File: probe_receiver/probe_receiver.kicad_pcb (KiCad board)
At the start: 2 copper layers, 32 x 32 mm, 9 parts, among them J1 Conn_01x05_Female, K1 HE721C0510, Q1 2N2907A, U1 TSSP4038

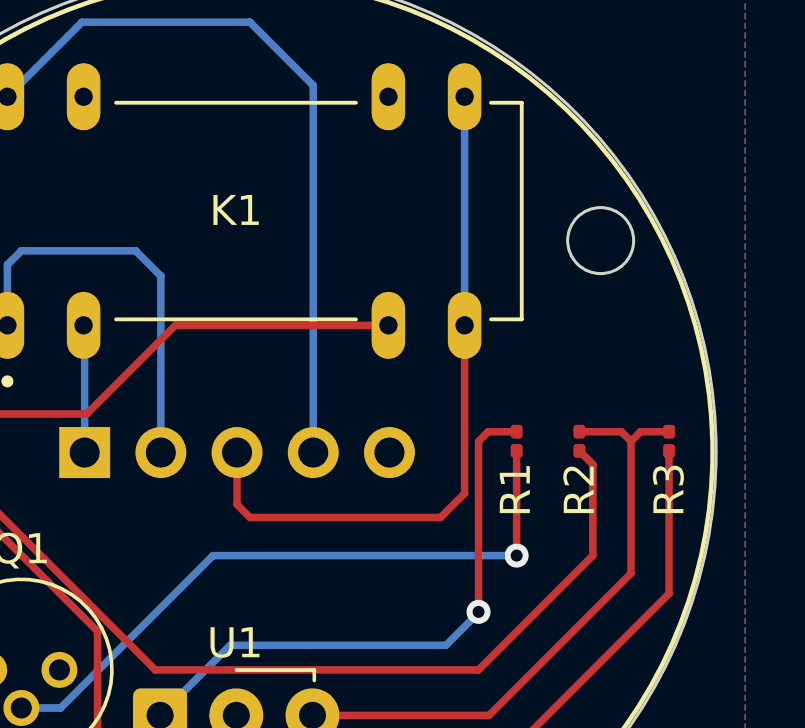
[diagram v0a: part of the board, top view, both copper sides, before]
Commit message: - add fix for PCB v1.1 (fix resistor place 1608)
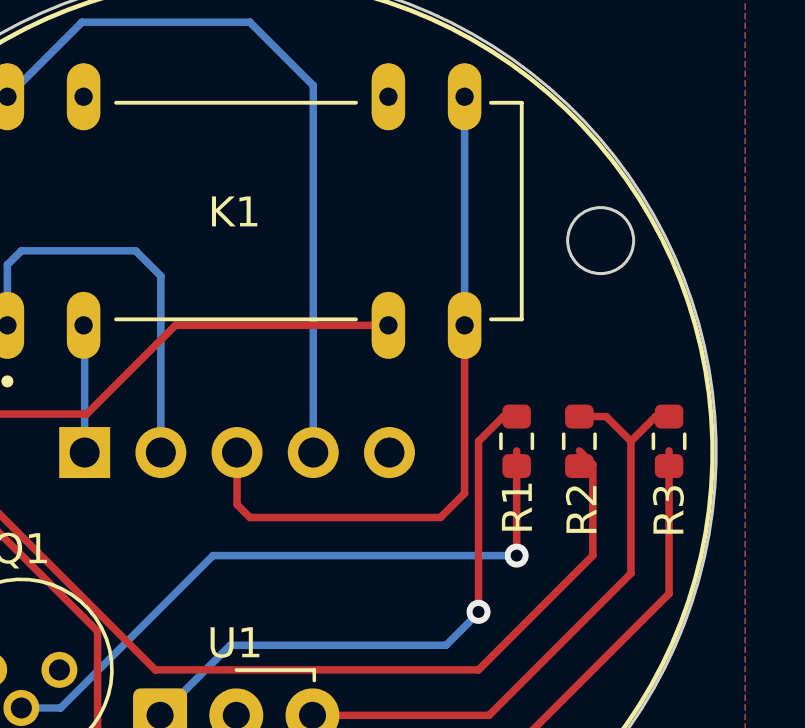
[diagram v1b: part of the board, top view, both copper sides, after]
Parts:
- added  : Probe Reciver v1.1, LOGO, B.Cu at (100.4, 89.2)
- R1, R2, R3: footprint Resistor_SMD:R_0201_0603Metric -> Resistor_SMD:R_0603_1608Metric

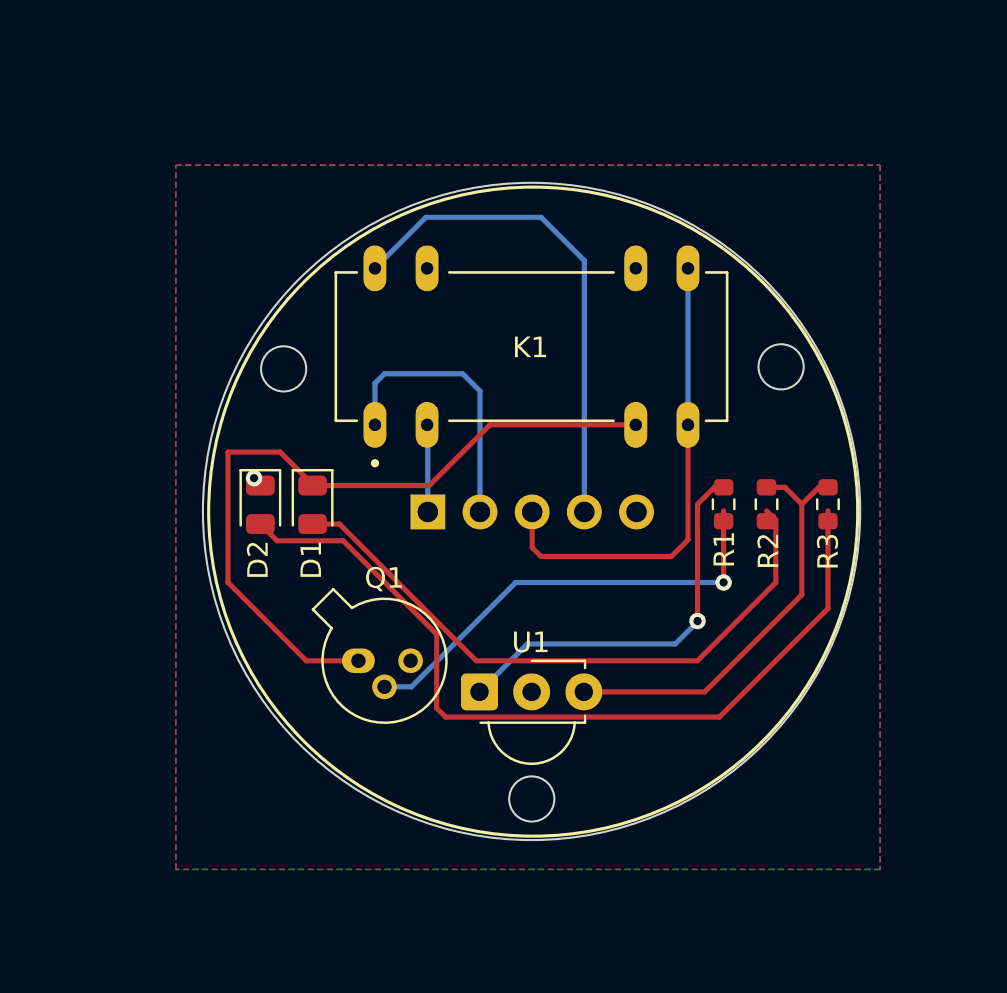
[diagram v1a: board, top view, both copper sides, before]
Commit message: - update probe reciver to v1.1
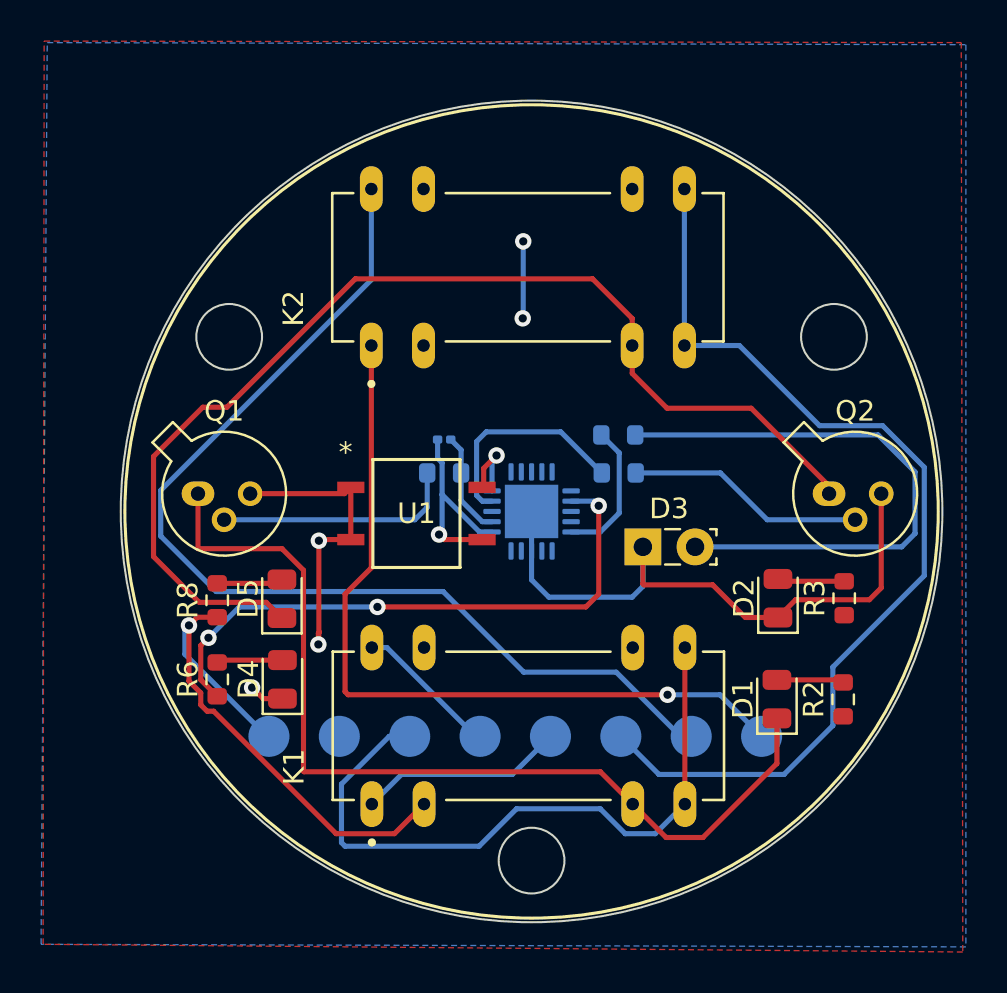
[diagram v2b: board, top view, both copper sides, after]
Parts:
- removed  : Probe Reciver v1.1, LOGO
- removed J1: Conn_01x05_Female, Connector_PinSocket_2.54mm:PinSocket_1x05_P2.54mm_Vertical
- added 5V1: TestPoint, TestPoint:TestPoint_Pad_D2.0mm, B.Cu at (87.2, 111.0)
- added D3: IRL81A, LED_THT:LED_SideEmitter_Rectangular_W4.5mm_H1.6mm, F.Cu at (105.4, 101.7)
- added D4: LED_YELLOW, LED_SMD:LED_0805_2012Metric, F.Cu at (87.9, 108.2)
- added D5: LED_ERR, LED_SMD:LED_0805_2012Metric, F.Cu at (87.8, 104.2)
- added EC1: TestPoint, TestPoint:TestPoint_Pad_D2.0mm, B.Cu at (111.2, 111.0)
- added EO1: TestPoint, TestPoint:TestPoint_Pad_D2.0mm, B.Cu at (107.8, 111.0)
- added ERR1: TestPoint, TestPoint:TestPoint_Pad_D2.0mm, B.Cu at (104.3, 111.0)
- added GND1: TestPoint, TestPoint:TestPoint_Pad_D2.0mm, B.Cu at (90.6, 111.0)
- added IN1: TestPoint, TestPoint:TestPoint_Pad_D2.0mm, B.Cu at (94.1, 111.0)
- added K2: HE721C0510, HE721C0510:RELAY_HE721C0510, F.Cu at (99.8, 88.1)
- added NC1: TestPoint, TestPoint:TestPoint_Pad_D2.0mm, B.Cu at (100.9, 111.0)
- added NO1: TestPoint, TestPoint:TestPoint_Pad_D2.0mm, B.Cu at (97.5, 111.0)
- added Q2: 2N2907A, Package_TO_SOT_THT:TO-18-3, F.Cu at (114.5, 99.1)
- added R4: R1K, Resistor_SMD:R_0603_1608Metric, B.Cu at (104.2, 96.3)
- added R5: R0, Resistor_SMD:R_0201_0603Metric, B.Cu at (95.7, 96.5)
- added R6: R1K, Resistor_SMD:R_0603_1608Metric, F.Cu at (84.7, 108.2)
- added R7: R39, Resistor_SMD:R_0603_1608Metric, B.Cu at (104.2, 98.1)
- added R8: R1K, Resistor_SMD:R_0603_1608Metric, F.Cu at (84.7, 104.3)
- added U2: ATtiny85-20M, Package_DFN_QFN:QFN-20-1EP_4x4mm_P0.5mm_EP2.6x2.6mm, B.Cu at (100.0, 100.0)
- D1: value LED -> LED_SIGN
- D2: value LED -> LED_POW
- R1: moved to B.Cu
- U1: value TSSP4038 -> IRM-H638T/TR2; footprint OptoDevice:Vishay_MINICAST-3Pin -> IRM-H638T-TR2:IRM-H638T&slash_TR2_EVE
- moved D2 25.6 mm to (112.0, 104.2), turned to 90 degrees
- moved D1 24.5 mm to (111.9, 109.1), turned to 90 degrees
- moved K1 18.5 mm to (99.8, 110.4)
- moved R1 13.7 mm to (95.7, 98.1), turned to 180 degrees
- moved Q1 11.3 mm to (83.8, 99.1)
- moved R2 10.2 mm to (115.2, 109.2), turned to 90 degrees
- moved U1 9.21 mm to (94.4, 100.1)
- moved R3 4.64 mm to (115.2, 104.2), turned to 90 degrees
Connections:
- U1 pad 1: Net-(R1-Pad1) -> GND
- U1 pad 3: +5V -> Net-(R5-Pad1)
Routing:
- net Net-(D5-Pad1): track 0.00 -> 55.0 mm
- net Net-(K2-Pad14): track 0.00 -> 51.0 mm
- net Net-(K2-Pad7): track 0.00 -> 48.3 mm
- net GND: track 0.00 -> 47.0 mm, vias 1 -> 3
- net Net-(K2-Pad1): track 0.00 -> 38.6 mm, vias 0 -> 1
- net Net-(D2-Pad2): track 40.6 -> 3.27 mm
- net Net-(R6-Pad1): track 0.00 -> 29.0 mm, vias 0 -> 3
- net Net-(R4-Pad2): track 0.00 -> 28.4 mm
- net Net-(D1-Pad2): track 30.6 -> 3.28 mm
- net Net-(K1-Pad14): track 24.3 -> 7.06 mm
- net Net-(R1-Pad1): track 19.4 -> 5.11 mm, vias 1 -> 0
- net Net-(Q2-Pad2): track 0.00 -> 11.6 mm
- net Net-(R7-Pad1): track 0.00 -> 10.6 mm
- net Net-(K1-Pad7): track 23.1 -> 33.4 mm
- net Net-(Q1-Pad2): track 22.1 -> 11.8 mm, vias 1 -> 0
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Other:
- board size 32 x 32 mm -> 40 x 40 mm

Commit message: - v .1.1 in prode
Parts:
- added  : Receiver Probe v1.1, LOGO, B.Cu at (100.4, 89.1)
- moved R2 0.98 mm to (115.2, 108.2)
- moved D1 0.96 mm to (111.9, 108.2)
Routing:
- net Net-(D1-Pad1): track 46.1 -> 47.1 mm
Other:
- outline, holes or cut-outs redrawn
- board text added: "ERR"
- board text added: "LOW"
- board text added: "POW"
- board text added: "TOUCH"
